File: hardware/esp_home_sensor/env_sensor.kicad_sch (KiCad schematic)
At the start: 5 parts, among them U7 BME680

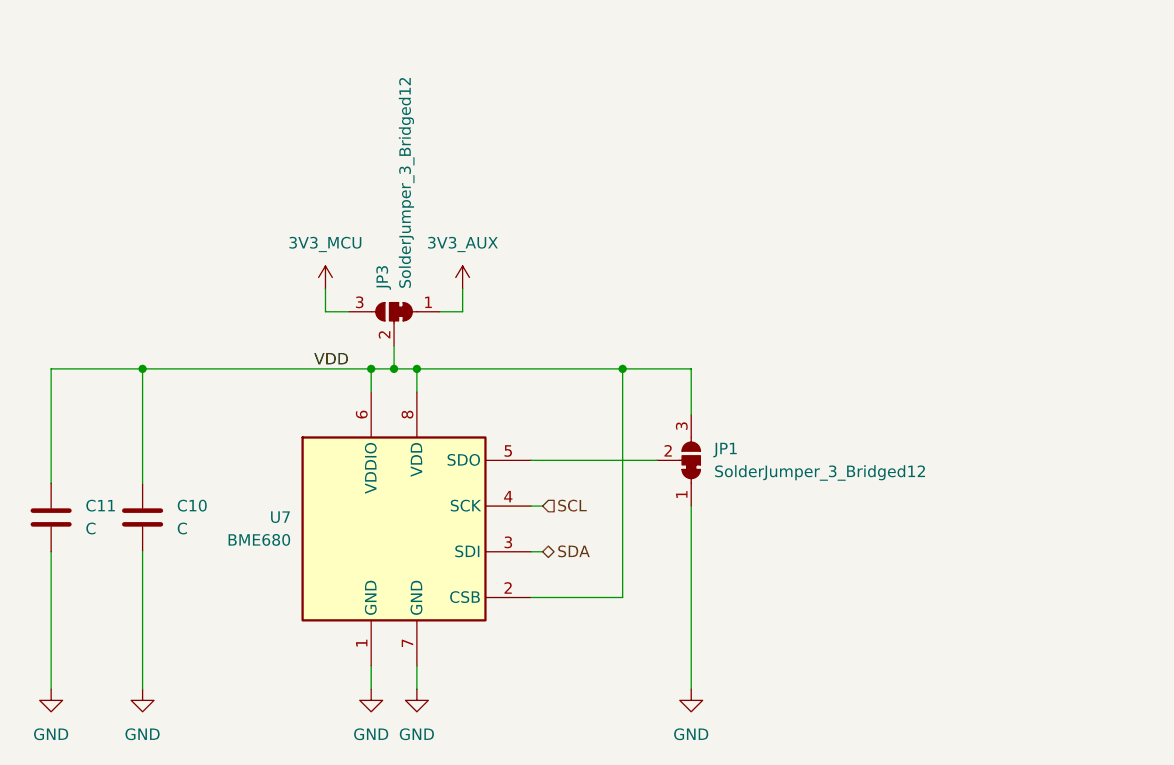
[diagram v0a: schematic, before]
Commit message: busses, display connector, footprint lib
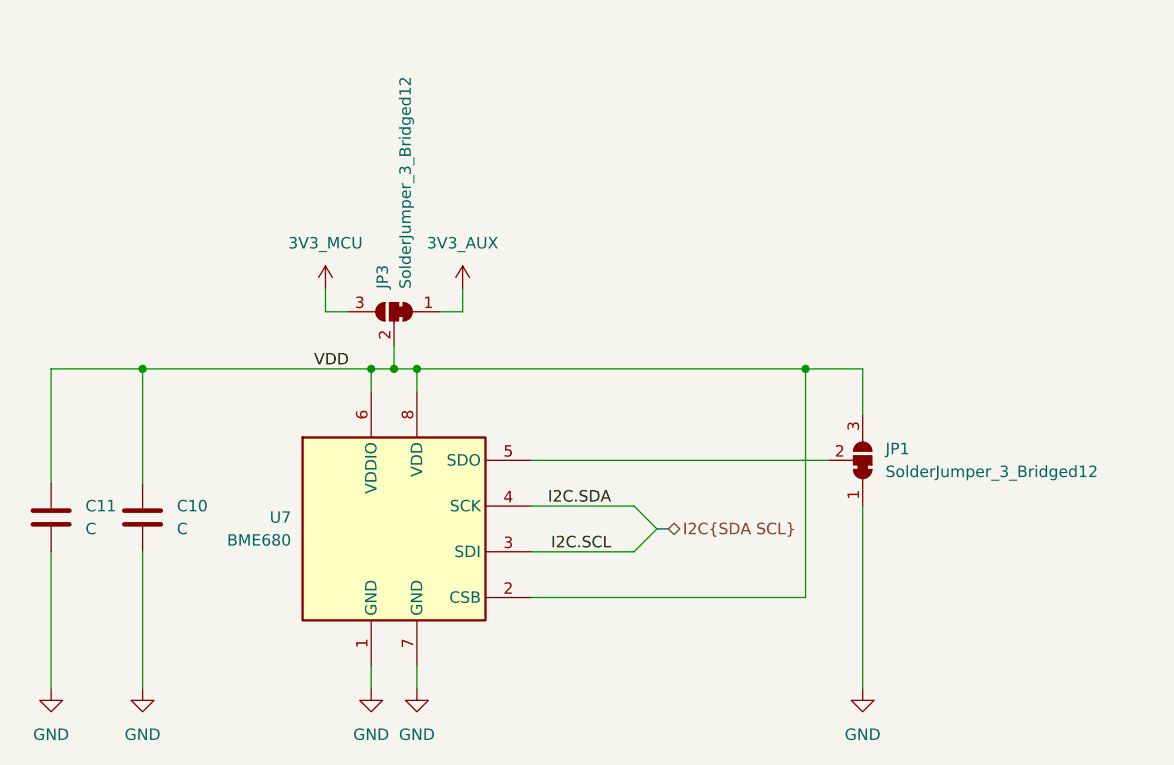
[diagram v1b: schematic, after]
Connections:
- net SCL renamed I2C.SDA
- net SDA renamed I2C.SCL
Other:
- moved on the sheet: JP1
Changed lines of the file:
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@@
-	)
-	(junction
-		(at 166.37 83.82)
-		(diameter 0)
-		(color 0 0 0 0)
 	)
 	(junction
@@
 		(color 0 0 0 0)
 	)
+	(junction
+		(at 186.69 83.82)
+		(diameter 0)
+		(color 0 0 0 0)
+	)
+	(bus_entry
+		(at 170.18 101.6)
+		(size -2.54 -2.54)
+		(stroke
+			(width 0)
+			(type default)
+		)
+	)
+	(bus_entry
+		(at 170.18 101.6)
+		(size -2.54 2.54)
+		(stroke
+			(width 0)
+			(type default)
+		)
+	)
 	(wire
 		(pts
@@
 	(wire
 		(pts
-			(xy 156.21 109.22) (xy 166.37 109.22)
-		)
-		(stroke
-			(width 0)
-			(type default)
-		)
-	)
-	(wire
-		(pts
-			(xy 143.51 83.82) (xy 166.37 83.82)
+			(xy 156.21 109.22) (xy 186.69 109.22)
+		)
+		(stroke
+			(width 0)
+			(type default)
+		)
+	)
+	(wire
+		(pts
+			(xy 143.51 83.82) (xy 186.69 83.82)
 		)
 		(stroke
@@
 	(wire
 		(pts
-			(xy 156.21 104.14) (xy 157.48 104.14)
-		)
-		(stroke
-			(width 0)
-			(type default)
-		)
-	)
-	(wire
-		(pts
-			(xy 156.21 93.98) (xy 170.18 93.98)
-		)
-		(stroke
-			(width 0)
-			(type default)
-		)
-	)
-	(wire
-		(pts
-			(xy 166.37 83.82) (xy 173.99 83.82)
+			(xy 156.21 104.14) (xy 167.64 104.14)
+		)
+		(stroke
+			(width 0)
+			(type default)
+		)
+	)
+	(wire
+		(pts
+			(xy 156.21 93.98) (xy 189.23 93.98)
 		)
 		(stroke
@@
 	(wire
 		(pts
-			(xy 156.21 99.06) (xy 157.48 99.06)
+			(xy 156.21 99.06) (xy 167.64 99.06)
 		)
 		(stroke
@@
 	(wire
 		(pts
-			(xy 173.99 99.06) (xy 173.99 119.38)
+			(xy 193.04 99.06) (xy 193.04 119.38)
 		)
 		(stroke
@@
 	(wire
 		(pts
-			(xy 166.37 83.82) (xy 166.37 109.22)
+			(xy 186.69 83.82) (xy 193.04 83.82)
+		)
+		(stroke
+			(width 0)
+			(type default)
+		)
+	)
+	(wire
+		(pts
+			(xy 186.69 83.82) (xy 186.69 109.22)
 		)
 		(stroke
@@
 	(wire
 		(pts
-			(xy 173.99 83.82) (xy 173.99 88.9)
+			(xy 193.04 83.82) (xy 193.04 88.9)
 		)
 		(stroke
@@
 		(pts
 			(xy 102.87 83.82) (xy 113.03 83.82)
+		)
+		(stroke
+			(width 0)
+			(type default)
+		)
+	)
+	(bus
+		(pts
+			(xy 170.18 101.6) (xy 171.45 101.6)
 		)
 		(stroke
@@
 		)
 	)
-	(hierarchical_label "SCL"
-		(shape input)
-		(at 157.48 99.06 0)
+	(label "I2C.SCL"
+		(at 165.1 104.14 180)
 		(effects
 			(font
 				(size 1.27 1.27)
 			)
-			(justify left)
-		)
-	)
-	(hierarchical_label "SDA"
+			(justify right bottom)
+		)
+	)
+	(label "I2C.SDA"
+		(at 165.1 99.06 180)
+		(effects
+			(font
+				(size 1.27 1.27)
+			)
+			(justify right bottom)
+		)
+	)
+	(hierarchical_label "I2C{SDA SCL}"
 		(shape bidirectional)
-		(at 157.48 104.14 0)
+		(at 171.45 101.6 0)
 		(effects
 			(font
@@
 	(symbol
 		(lib_id "power:GND")
-		(at 173.99 119.38 0)
+		(at 193.04 119.38 0)
 		(mirror y)
 		(unit 1)
@@
 		(dnp no)
 		(property "Reference" "#PWR024"
-			(at 173.99 125.73 0)
+			(at 193.04 125.73 0)
 			(hide yes)
 			(show_name no)
@@
 		)
 		(property "Value" "GND"
-			(at 173.99 124.46 0)
+			(at 193.04 124.46 0)
 			(show_name no)
 			(do_not_autoplace no)
@@
 		)
 		(property "Footprint" ""
-			(at 173.99 119.38 0)
+			(at 193.04 119.38 0)
 			(hide yes)
 			(show_name no)
@@
 		)
 		(property "Datasheet" ""
-			(at 173.99 119.38 0)
+			(at 193.04 119.38 0)
 			(hide yes)
 			(show_name no)
@@
 		)
 		(property "Description" "Power symbol creates a global label with name \"GND\" , ground"
-			(at 173.99 119.38 0)
+			(at 193.04 119.38 0)
 			(hide yes)
 			(show_name no)
@@
 	(symbol
 		(lib_id "Jumper:SolderJumper_3_Bridged12")
-		(at 173.99 93.98 270)
+		(at 193.04 93.98 270)
 		(mirror x)
 		(unit 1)
@@
 		(fields_autoplaced yes)
 		(property "Reference" "JP1"
-			(at 176.53 92.7099 90)
+			(at 195.58 92.7099 90)
 			(show_name no)
 			(do_not_autoplace no)
@@
 		)
 		(property "Value" "SolderJumper_3_Bridged12"
-			(at 176.53 95.2499 90)
+			(at 195.58 95.2499 90)
 			(show_name no)
 			(do_not_autoplace no)
@@
 		)
 		(property "Footprint" ""
-			(at 173.99 93.98 0)
+			(at 193.04 93.98 0)
 			(hide yes)
 			(show_name no)
@@
 		)
 		(property "Datasheet" ""
-			(at 158.75 93.98 0)
+			(at 177.8 93.98 0)
 			(hide yes)
 			(show_name no)
@@
 		)
 		(property "Description" "3-pole Solder Jumper, pins 1+2 closed/bridged"
-			(at 161.29 93.98 0)
-			(hide yes)
-			(show_name no)
+			(at 180.34 93.98 0)
+			(hide yes)
+			(show_name no)

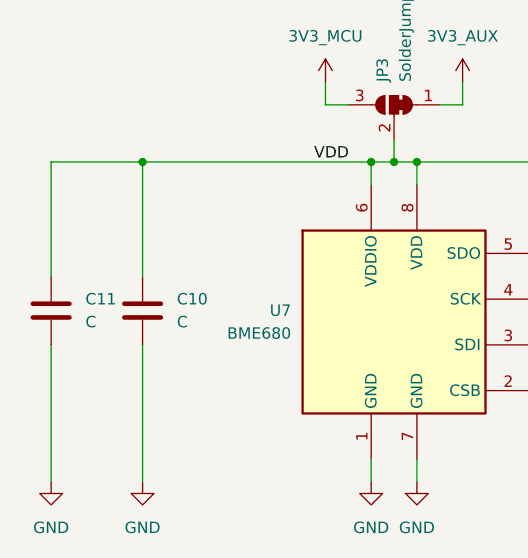
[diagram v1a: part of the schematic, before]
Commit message: footprint assignment, buck
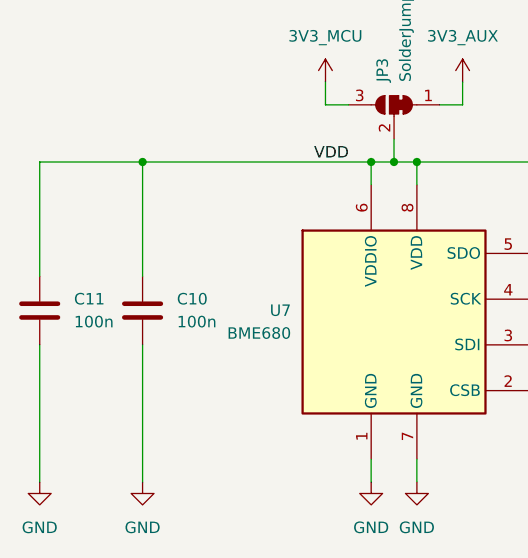
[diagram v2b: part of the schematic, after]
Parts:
- C10, C11: value C -> 100n; footprint (none) -> Capacitor_SMD:C_0402_1005Metric
- U7: Mfr. No. (none) -> BME680
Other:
- moved on the sheet: C11
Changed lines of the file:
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@@
+	)
+	(junction
+		(at 113.03 83.82)
+		(diameter 0)
+		(color 0 0 0 0)
 	)
 	(junction
@@
 	)
 	(junction
-		(at 113.03 83.82)
-		(diameter 0)
-		(color 0 0 0 0)
-	)
-	(junction
 		(at 186.69 83.82)
 		(diameter 0)
@@
 	(wire
 		(pts
-			(xy 102.87 104.14) (xy 102.87 119.38)
+			(xy 101.6 104.14) (xy 101.6 119.38)
 		)
 		(stroke
@@
 	(wire
 		(pts
-			(xy 102.87 96.52) (xy 102.87 83.82)
+			(xy 101.6 96.52) (xy 101.6 83.82)
 		)
 		(stroke
@@
 	(wire
 		(pts
-			(xy 102.87 83.82) (xy 113.03 83.82)
+			(xy 101.6 83.82) (xy 113.03 83.82)
 		)
 		(stroke
@@
 			)
 		)
+		(property "Mfr. No." ""
+			(at 140.97 77.47 90)
+			(hide yes)
+			(show_name no)
+			(do_not_autoplace no)
+			(effects
+				(font
+					(size 1.27 1.27)
+				)
+			)
+		)
 		(pin "3"
 		)
@@
 	(symbol
 		(lib_id "power:GND")
-		(at 102.87 119.38 0)
+		(at 101.6 119.38 0)
 		(mirror y)
 		(unit 1)
@@
 		(dnp no)
 		(property "Reference" "#PWR027"
-			(at 102.87 125.73 0)
+			(at 101.6 125.73 0)
 			(hide yes)
 			(show_name no)
@@
 		)
 		(property "Value" "GND"
-			(at 102.87 124.46 0)
+			(at 101.6 124.46 0)
 			(show_name no)
 			(do_not_autoplace no)
@@
 		)
 		(property "Footprint" ""
-			(at 102.87 119.38 0)
+			(at 101.6 119.38 0)
 			(hide yes)
 			(show_name no)
@@
 		)
 		(property "Datasheet" ""
-			(at 102.87 119.38 0)
+			(at 101.6 119.38 0)
 			(hide yes)
 			(show_name no)
@@
 		)
 		(property "Description" "Power symbol creates a global label with name \"GND\" , ground"
-			(at 102.87 119.38 0)
+			(at 101.6 119.38 0)
 			(hide yes)
 			(show_name no)
@@
 			)
 		)
+		(property "Mfr. No." ""
+			(at 193.04 93.98 90)
+			(hide yes)
+			(show_name no)
+			(do_not_autoplace no)
+			(effects
+				(font
+					(size 1.27 1.27)
+				)
+			)
+		)
 		(pin "3"
 		)
@@
 	(symbol
 		(lib_id "Device:C")
-		(at 102.87 100.33 0)
+		(at 101.6 100.33 0)
 		(unit 1)
 		(body_style 1)
@@
 		(fields_autoplaced yes)
 		(property "Reference" "C11"
-			(at 106.68 99.0599 0)
+			(at 105.41 99.0599 0)
 			(show_name no)
 			(do_not_autoplace no)
@@
 			)
 		)
-		(property "Value" "C"
-			(at 106.68 101.5999 0)
+		(property "Value" "100n"
+			(at 105.41 101.5999 0)
 			(show_name no)
 			(do_not_autoplace no)
@@
 			)
 		)
-		(property "Footprint" ""
-			(at 103.8352 104.14 0)
+		(property "Footprint" "Capacitor_SMD:C_0402_1005Metric"
+			(at 102.5652 104.14 0)
 			(hide yes)
 			(show_name no)
@@
 		)
 		(property "Datasheet" ""
-			(at 102.87 100.33 0)
+			(at 101.6 100.33 0)
 			(hide yes)
 			(show_name no)
@@
 		)
 		(property "Description" "Unpolarized capacitor"
-			(at 102.87 100.33 0)
+			(at 101.6 100.33 0)
+			(hide yes)
+			(show_name no)
+			(do_not_autoplace no)
+			(effects
+				(font
+					(size 1.27 1.27)
+				)
+			)
+		)
+		(property "Mfr. No." ""
+			(at 101.6 100.33 0)
 			(hide yes)
 			(show_name no)
@@
 			)
 		)
-		(property "Value" "C"
+		(property "Value" "100n"
 			(at 116.84 101.5999 0)
 			(show_name no)
@@
 			)
 		)
-		(property "Footprint" ""
+		(property "Footprint" "Capacitor_SMD:C_0402_1005Metric"
 			(at 113.9952 104.14 0)
 			(hide yes)
@@
 		)
 		(property "Description" "Unpolarized capacitor"
+			(at 113.03 100.33 0)
+			(hide yes)
+			(show_name no)
+			(do_not_autoplace no)
+			(effects
+				(font
+					(size 1.27 1.27)
+				)
+			)
+		)
+		(property "Mfr. No." ""
 			(at 113.03 100.33 0)
 			(hide yes)
@@
 			(at 140.97 101.6 0)
 			(hide yes)
+			(show_name no)
+			(do_not_autoplace no)
+			(effects
+				(font
+					(size 1.27 1.27)
+				)
+			)
+		)
+		(property "Mfr. No." "BME680 "
+			(at 140.97 101.6 0)
+			(hide yes)

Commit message: minor update
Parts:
- JP1, JP3: footprint (none) -> Jumper:SolderJumper-3_P1.3mm_Bridged12_Pad1.0x1.5mm
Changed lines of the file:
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@@
 			)
 		)
-		(property "Footprint" ""
+		(property "Footprint" "Jumper:SolderJumper-3_P1.3mm_Bridged12_Pad1.0x1.5mm"
 			(at 140.97 77.47 0)
 			(hide yes)
@@
 			)
 		)
-		(property "Footprint" ""
+		(property "Footprint" "Jumper:SolderJumper-3_P1.3mm_Bridged12_Pad1.0x1.5mm"
 			(at 193.04 93.98 0)
 			(hide yes)

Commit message: initial layout, power routing
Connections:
- net sdo: now reaches JP1.2 (C), U7.5 (SDO)
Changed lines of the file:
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@@
+		)
+	)
+	(label "sdo"
+		(at 165.1 93.98 180)
+		(effects
+			(font
+				(size 1.27 1.27)
+			)
+			(justify right bottom)
 		)
 	)

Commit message: layout
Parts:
- renumbered C11 to C14, C10 to C15, JP3 to JP4, JP1 to JP5
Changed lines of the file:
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@@
 		(in_pos_files yes)
 		(dnp no)
-		(property "Reference" "JP3"
+		(property "Reference" "JP4"
 			(at 139.6999 74.93 90)
 			(show_name no)
@@
 			(project "esp_home_sensor"
 				(path "/1b1bee14-8d82-405b-b99d-415549a137e6/3b3a610d-7469-4392-abd9-583ce25d17a3"
-					(reference "JP3")
+					(reference "JP4")
 					(unit 1)
 				)
@@
 		(in_pos_files yes)
 		(dnp no)
-		(property "Reference" "#PWR027"
+		(property "Reference" "#PWR043"
 			(at 101.6 125.73 0)
 			(hide yes)
@@
 			(project "esp_home_sensor"
 				(path "/1b1bee14-8d82-405b-b99d-415549a137e6/3b3a610d-7469-4392-abd9-583ce25d17a3"
-					(reference "#PWR027")
+					(reference "#PWR043")
 					(unit 1)
 				)
@@
 		(in_pos_files yes)
 		(dnp no)
-		(property "Reference" "#PWR023"
+		(property "Reference" "#PWR047"
 			(at 143.51 125.73 0)
 			(hide yes)
@@
 			(project "esp_home_sensor"
 				(path "/1b1bee14-8d82-405b-b99d-415549a137e6/3b3a610d-7469-4392-abd9-583ce25d17a3"
-					(reference "#PWR023")
+					(reference "#PWR047")
 					(unit 1)
 				)
@@
 		(in_pos_files yes)
 		(dnp no)
-		(property "Reference" "#PWR024"
+		(property "Reference" "#PWR049"
 			(at 193.04 125.73 0)
 			(hide yes)
@@
 			(project "esp_home_sensor"
 				(path "/1b1bee14-8d82-405b-b99d-415549a137e6/3b3a610d-7469-4392-abd9-583ce25d17a3"
-					(reference "#PWR024")
+					(reference "#PWR049")
 					(unit 1)
 				)
@@
 		(dnp no)
 		(fields_autoplaced yes)
-		(property "Reference" "JP1"
+		(property "Reference" "JP5"
 			(at 195.58 92.7099 90)
 			(show_name no)
@@
 			(project "esp_home_sensor"
 				(path "/1b1bee14-8d82-405b-b99d-415549a137e6/3b3a610d-7469-4392-abd9-583ce25d17a3"
-					(reference "JP1")
+					(reference "JP5")
 					(unit 1)
 				)
@@
 		(in_pos_files yes)
 		(dnp no)
-		(property "Reference" "#PWR022"
+		(property "Reference" "#PWR046"
 			(at 138.43 125.73 0)
 			(hide yes)
@@
 			(project "esp_home_sensor"
 				(path "/1b1bee14-8d82-405b-b99d-415549a137e6/3b3a610d-7469-4392-abd9-583ce25d17a3"
-					(reference "#PWR022")
+					(reference "#PWR046")
 					(unit 1)
 				)
@@
 		(dnp no)
 		(fields_autoplaced yes)
-		(property "Reference" "C11"
+		(property "Reference" "C14"
 			(at 105.41 99.0599 0)
 			(show_name no)
@@
 			(project "esp_home_sensor"
 				(path "/1b1bee14-8d82-405b-b99d-415549a137e6/3b3a610d-7469-4392-abd9-583ce25d17a3"
-					(reference "C11")
+					(reference "C14")
 					(unit 1)
 				)
@@
 		(dnp no)
 		(fields_autoplaced yes)
-		(property "Reference" "C10"
+		(property "Reference" "C15"
 			(at 116.84 99.0599 0)
 			(show_name no)
@@
 			(project "esp_home_sensor"
 				(path "/1b1bee14-8d82-405b-b99d-415549a137e6/3b3a610d-7469-4392-abd9-583ce25d17a3"
-					(reference "C10")
+					(reference "C15")
 					(unit 1)
 				)
@@
 		(dnp no)
 		(fields_autoplaced yes)
-		(property "Reference" "#PWR038"
+		(property "Reference" "#PWR045"
 			(at 133.35 78.74 0)
 			(hide yes)
@@
 			(project "esp_home_sensor"
 				(path "/1b1bee14-8d82-405b-b99d-415549a137e6/3b3a610d-7469-4392-abd9-583ce25d17a3"
-					(reference "#PWR038")
+					(reference "#PWR045")
 					(unit 1)
 				)
@@
 		(dnp no)
 		(fields_autoplaced yes)
-		(property "Reference" "#PWR025"
+		(property "Reference" "#PWR048"
 			(at 148.59 78.74 0)
 			(hide yes)
@@
 			(project "esp_home_sensor"
 				(path "/1b1bee14-8d82-405b-b99d-415549a137e6/3b3a610d-7469-4392-abd9-583ce25d17a3"
-					(reference "#PWR025")
+					(reference "#PWR048")
 					(unit 1)
 				)
@@
 		(in_pos_files yes)
 		(dnp no)
-		(property "Reference" "#PWR026"
+		(property "Reference" "#PWR044"
 			(at 113.03 125.73 0)
 			(hide yes)
@@
 			(project "esp_home_sensor"
 				(path "/1b1bee14-8d82-405b-b99d-415549a137e6/3b3a610d-7469-4392-abd9-583ce25d17a3"
-					(reference "#PWR026")
-					(unit 1)
-				)
+					(reference "#PWR044")
+					(unit 1)
+				)

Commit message: in production
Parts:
- C14, C15: Mfr. No. (none) -> GRM155R71H104KE14D
- U7: Mfr. No. BME680 -> BME680
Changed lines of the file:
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@@
 			)
 		)
-		(property "Mfr. No." ""
+		(property "Mfr. No." "GRM155R71H104KE14D"
 			(at 101.6 100.33 0)
 			(hide yes)
@@
 			)
 		)
-		(property "Mfr. No." ""
+		(property "Mfr. No." "GRM155R71H104KE14D"
 			(at 113.03 100.33 0)
 			(hide yes)
@@
 			)
 		)
-		(property "Mfr. No." "BME680 "
+		(property "Mfr. No." "BME680"
 			(at 140.97 101.6 0)
 			(hide yes)

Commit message: az
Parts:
- U7: Down_current (none) -> 150n; Supply_current (none) -> 1.3m
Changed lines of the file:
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@@
+			)
+		)
+		(property "Down_current" ""
+			(at 140.97 77.47 90)
+			(hide yes)
+			(show_name no)
+			(do_not_autoplace no)
+			(effects
+				(font
+					(size 1.27 1.27)
+				)
+			)
+		)
+		(property "Supply_current" ""
+			(at 140.97 77.47 90)
+			(hide yes)
+			(show_name no)
+			(do_not_autoplace no)
+			(effects
+				(font
+					(size 1.27 1.27)
+				)
 			)
 		)
@@
 			)
 		)
+		(property "Down_current" ""
+			(at 193.04 93.98 90)
+			(hide yes)
+			(show_name no)
+			(do_not_autoplace no)
+			(effects
+				(font
+					(size 1.27 1.27)
+				)
+			)
+		)
+		(property "Supply_current" ""
+			(at 193.04 93.98 90)
+			(hide yes)
+			(show_name no)
+			(do_not_autoplace no)
+			(effects
+				(font
+					(size 1.27 1.27)
+				)
+			)
+		)
 		(pin "3"
 		)
@@
 			)
 		)
+		(property "Down_current" ""
+			(at 101.6 100.33 0)
+			(hide yes)
+			(show_name no)
+			(do_not_autoplace no)
+			(effects
+				(font
+					(size 1.27 1.27)
+				)
+			)
+		)
+		(property "Supply_current" ""
+			(at 101.6 100.33 0)
+			(hide yes)
+			(show_name no)
+			(do_not_autoplace no)
+			(effects
+				(font
+					(size 1.27 1.27)
+				)
+			)
+		)
 		(pin "2"
 		)
@@
 			)
 		)
+		(property "Down_current" ""
+			(at 113.03 100.33 0)
+			(hide yes)
+			(show_name no)
+			(do_not_autoplace no)
+			(effects
+				(font
+					(size 1.27 1.27)
+				)
+			)
+		)
+		(property "Supply_current" ""
+			(at 113.03 100.33 0)
+			(hide yes)
+			(show_name no)
+			(do_not_autoplace no)
+			(effects
+				(font
+					(size 1.27 1.27)
+				)
+			)
+		)
 		(pin "2"
 		)
@@
 			(at 140.97 101.6 0)
 			(hide yes)
+			(show_name no)
+			(do_not_autoplace no)
+			(effects
+				(font
+					(size 1.27 1.27)
+				)
+			)
+		)
+		(property "Down_current" "150n"
+			(at 140.97 101.6 0)
+			(hide yes)
+			(show_name no)
+			(do_not_autoplace no)
+			(effects
+				(font
+					(size 1.27 1.27)
+				)
+			)
+		)
+		(property "Supply_current" "1.3m"
+			(at 140.97 101.6 0)
+			(hide yes)
